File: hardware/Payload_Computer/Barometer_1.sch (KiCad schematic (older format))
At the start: 3 parts

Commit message: Minor changes
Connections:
- net SDI renamed MOSI
- net SDO renamed MISO
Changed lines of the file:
@@
 $Descr A4 11693 8268
 encoding utf-8
-Sheet 26 27
+Sheet 27 27
 Title ""
 Date ""
@@
 Comment4 ""
 $EndDescr
-$Comp
-L Payload_Computer-cache:+3.3V #PWR?
-U 1 1 5FDAA6E0
-P 5710 2860
-F 0 "#PWR?" H 5710 2710 50  0001 C CNN
-F 1 "+3.3V" H 5740 3000 50  0000 C CNN
-F 2 "" H 5710 2860 50  0001 C CNN
-F 3 "" H 5710 2860 50  0001 C CNN
-	1    5710 2860
-	1    0    0    -1
-$EndComp
-$Comp
-L Payload_Computer-cache:+3.3V #PWR?
-U 1 1 5FDAA855
-P 5510 2860
-F 0 "#PWR?" H 5510 2710 50  0001 C CNN
-F 1 "+3.3V" H 5470 3000 50  0000 C CNN
-F 2 "" H 5510 2860 50  0001 C CNN
-F 3 "" H 5510 2860 50  0001 C CNN
-	1    5510 2860
-	1    0    0    -1
-$EndComp
 $Comp
 L power:GND #PWR?
@@
 	5610 4550 5710 4550
 Text HLabel 6530 3520 2    50   Input ~ 0
-SDO
+MISO
 Text HLabel 6530 3720 2    50   Input ~ 0
 SCK
 Text HLabel 6530 3920 2    50   Input ~ 0
-SDI
+MOSI
 Text HLabel 6530 4120 2    50   Input ~ 0
 CSB
@@
 	1    0    0    -1
 $EndComp
+$Comp
+L power:+3.3V #PWR?
+U 1 1 5FE2FC03
+P 5510 2860
+F 0 "#PWR?" H 5510 2710 50  0001 C CNN
+F 1 "+3.3V" H 5525 3033 50  0000 C CNN
+F 2 "" H 5510 2860 50  0001 C CNN
+F 3 "" H 5510 2860 50  0001 C CNN
+	1    5510 2860
+	1    0    0    -1
+$EndComp
+$Comp
+L power:+3.3V #PWR?
+U 1 1 5FE30EDD
+P 5710 2860
+F 0 "#PWR?" H 5710 2710 50  0001 C CNN
+F 1 "+3.3V" H 5725 3033 50  0000 C CNN
+F 2 "" H 5710 2860 50  0001 C CNN
+F 3 "" H 5710 2860 50  0001 C CNN
+	1    5710 2860
+	1    0    0    -1
+$EndComp

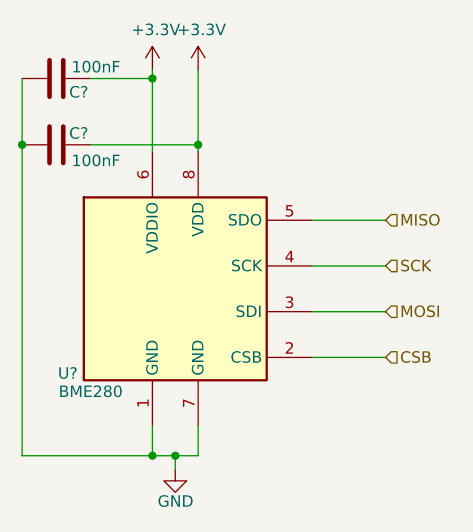
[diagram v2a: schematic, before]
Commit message: Finished Fan Schematic. Working on Servos
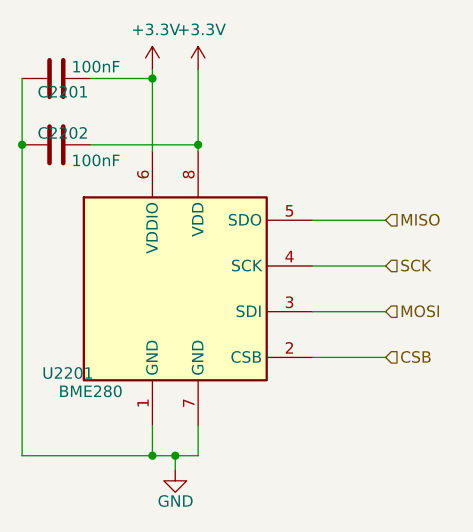
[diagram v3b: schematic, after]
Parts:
- C2201, C2202: renamed from C?; footprint (none) -> Capacitor_SMD:C_0603_1608Metric_Pad1.08x0.95mm_HandSolder
- gave numbers to parts that had none: 1
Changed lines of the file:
@@
 $Descr A4 11693 8268
 encoding utf-8
-Sheet 27 26
+Sheet 22 22
 Title ""
 Date ""
@@
 $EndDescr
 $Comp
-L power:GND #PWR?
+L power:GND #PWR02202
 U 1 1 5FDABC48
 P 5610 4610
-F 0 "#PWR?" H 5610 4360 50  0001 C CNN
+F 0 "#PWR02202" H 5610 4360 50  0001 C CNN
 F 1 "GND" H 5690 4470 50  0000 R CNN
 F 2 "" H 5610 4610 50  0001 C CNN
@@
 $EndComp
 $Comp
-L Device:C C?
+L Device:C C2202
 U 1 1 5FDACEC1
 P 5090 3190
-F 0 "C?" V 5140 3050 50  0000 L CNN
+F 0 "C2202" V 5140 3050 50  0000 L CNN
 F 1 "100nF" V 5020 2910 50  0000 L CNN
-F 2 "" H 5128 3040 50  0001 C CNN
+F 2 "Capacitor_SMD:C_0603_1608Metric_Pad1.08x0.95mm_HandSolder" H 5128 3040 50  0001 C CNN
 F 3 "~" H 5090 3190 50  0001 C CNN
 	1    5090 3190
@@
 	5510 2900 5240 2900
 $Comp
-L Device:C C?
+L Device:C C2201
 U 1 1 5FDAC53E
 P 5090 2900
-F 0 "C?" V 5030 2760 50  0000 L CNN
+F 0 "C2201" V 5030 2760 50  0000 L CNN
 F 1 "100nF" V 5140 2620 50  0000 L CNN
-F 2 "" H 5128 2750 50  0001 C CNN
+F 2 "Capacitor_SMD:C_0603_1608Metric_Pad1.08x0.95mm_HandSolder" H 5128 2750 50  0001 C CNN
 F 3 "~" H 5090 2900 50  0001 C CNN
 	1    5090 2900
@@
 CSB
 $Comp
-L Sensor:BME280 U?
+L Sensor:BME280 U2201
 U 1 1 5FDA9981
 P 5610 3820
-F 0 "U?" H 5140 3450 50  0000 C CNN
+F 0 "U2201" H 5140 3450 50  0000 C CNN
 F 1 "BME280" H 5240 3370 50  0000 C CNN
 F 2 "Package_LGA:Bosch_LGA-8_2.5x2.5mm_P0.65mm_ClockwisePinNumbering" H 7110 3370 50  0001 C CNN
@@
 $EndComp
 $Comp
-L power:+3.3V #PWR?
+L power:+3.3V #PWR02201
 U 1 1 5FE2FC03
 P 5510 2860
-F 0 "#PWR?" H 5510 2710 50  0001 C CNN
+F 0 "#PWR02201" H 5510 2710 50  0001 C CNN
 F 1 "+3.3V" H 5525 3033 50  0000 C CNN
 F 2 "" H 5510 2860 50  0001 C CNN
@@
 $EndComp
 $Comp
-L power:+3.3V #PWR?
+L power:+3.3V #PWR02203
 U 1 1 5FE30EDD
 P 5710 2860
-F 0 "#PWR?" H 5710 2710 50  0001 C CNN
+F 0 "#PWR02203" H 5710 2710 50  0001 C CNN
 F 1 "+3.3V" H 5725 3033 50  0000 C CNN
 F 2 "" H 5710 2860 50  0001 C CNN
